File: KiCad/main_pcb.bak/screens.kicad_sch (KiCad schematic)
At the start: 15 parts, among them J7 1X7 Header, J8 1X7 Header, J9 1x13 Header, U4 TI TXB0104DR, U6 TI TXB0104DR, U9 TI TXB0104DR

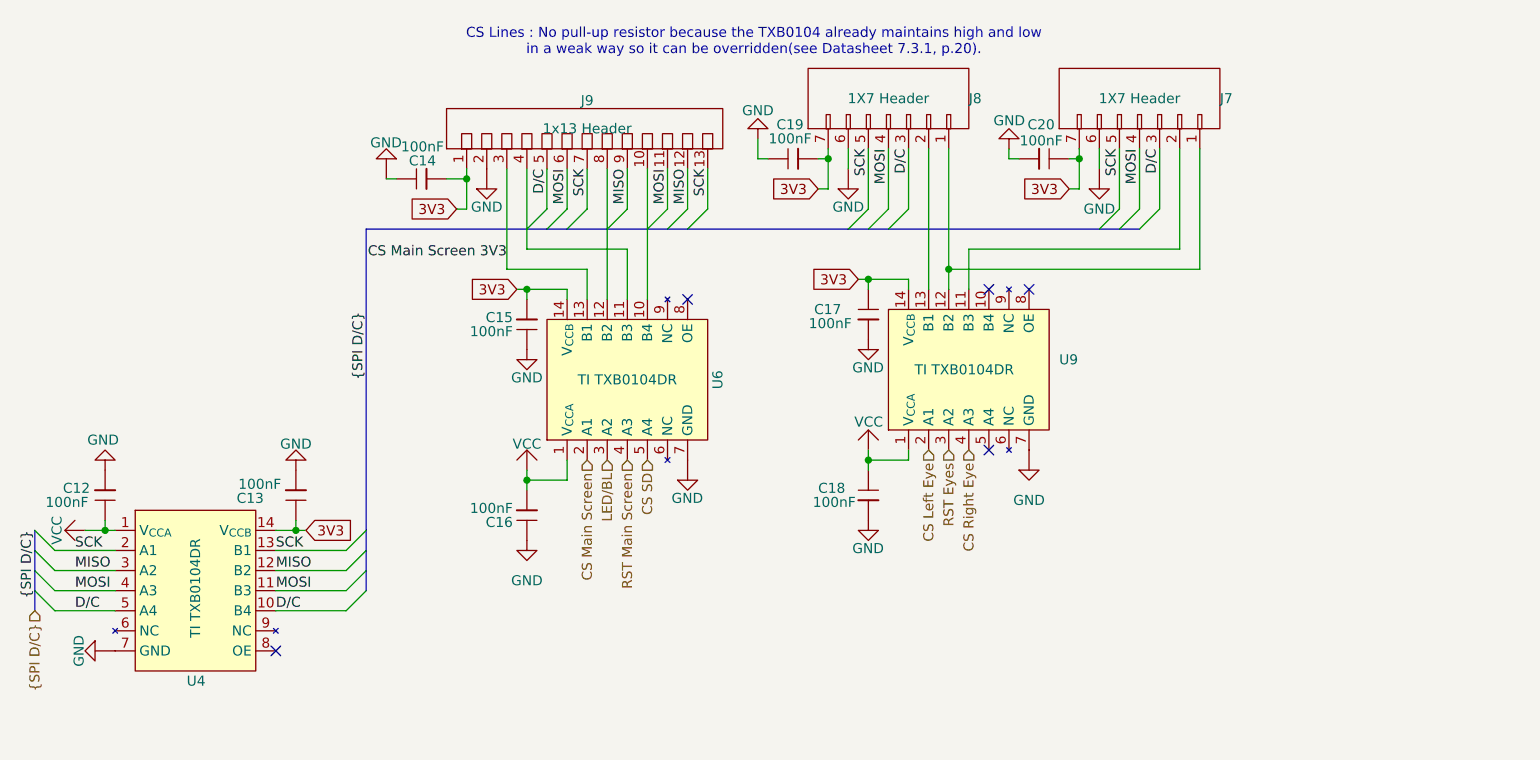
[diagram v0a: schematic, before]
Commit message: Maddie/main pcb refactor (#39)
* feat(PCB Layout): Refactors Main PCB layout to achieve smaller form factor and adds JLCPCB constraints.

* feat(symbols): Adds 4pin crystal symbols and adds it to schematic

* feat(schematic): Connects C2 and C3 to the crystal

* feat(schematic): Revamps fully the circuit schematic

* feat(schematic): Assigns footprints to symbols

* feat(pcb): Alternative first draft

* feat(pcb): Second draft

* feat(pdf): Updates schematic PDF

* feat(pdf): Updates schematic PDF

* chore(migration): Puts old layout in main_pcb.bak/ and new layout to main_pcb/

* feat(PCB): Updates PCB layout after Christian's review, thansk a lot Christian :) !
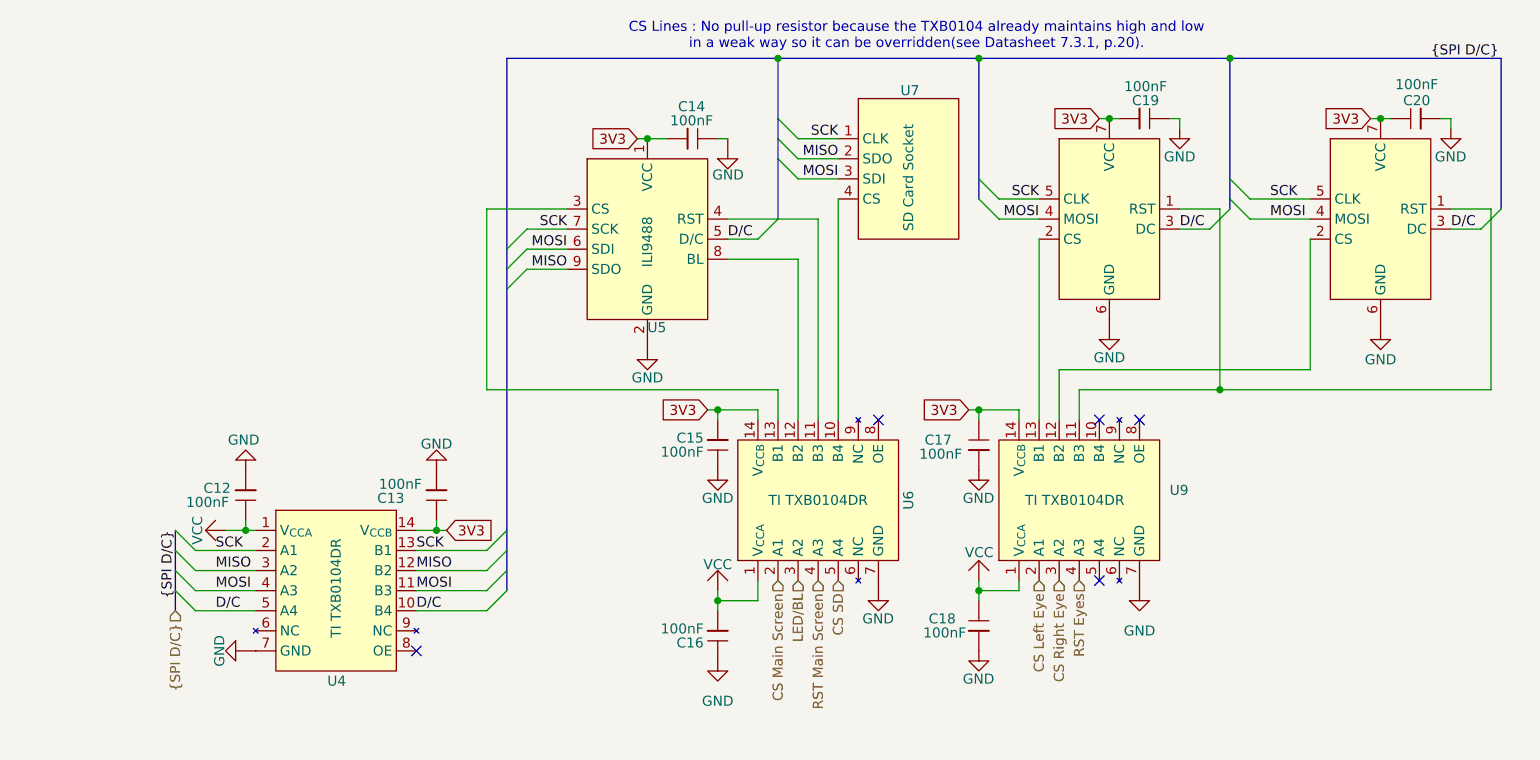
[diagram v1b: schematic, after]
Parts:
- removed J7, J8: 1X7 Header, Lilibrary:1x7 Header, symbol Lily's Pad:1x7_Header
- removed J9: 1x13 Header, Lilibrary:1x13 Header, symbol Lily's Pad:1x13_Header
- added U10, U8: ~, symbol Lily's Pad:GC9A01
- added U5: ILI9488, symbol Lily's Pad:ILI9488
- added U7: SD Card Socket, symbol Lily's Pad:SD_Card_Socket
- C12, C13, C14, C15, C16, C17, C18, C19, C20: footprint Capacitor_SMD:C_0603_1608Metric_Pad1.08x0.95mm_HandSolder -> Capacitor_SMD:C_0201_0603Metric_Pad0.64x0.40mm_HandSolder
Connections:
- net 3V3: now also U10.7 (VCC), U5.1 (VCC), U8.7 (VCC)
- net CS Right Eye: now also U9.3 (A2); no longer U9.4 (A3)
- net D/C: now also U10.3 (DC), U5.5 (D/C), U8.3 (DC)
- net GND: now also U10.6 (GND), U5.2 (GND), U8.6 (GND)
- net MISO: now also U5.9 (SDO), U7.2 (SDO)
- net MOSI: now also U10.4 (MOSI), U5.6 (SDI), U7.3 (SDI), U8.4 (MOSI)
- net RST Eyes: now also U9.4 (A3); no longer U9.3 (A2)
- net SCK: now also U10.5 (CLK), U5.7 (SCK), U7.1 (CLK), U8.5 (CLK)
- net at U9.11 (B3): now also U10.1 (RST), U8.1 (RST)
- net at U9.12 (B2): now also U10.2 (CS)
- net at U9.13 (B1): now also U8.2 (CS)
- net at U6.10 (B4): now also U7.4 (CS)
- net at U6.11 (B3): now also U5.4 (RST)
- net at U6.12 (B2): now also U5.8 (BL)
- net CS Main Screen 3V3: no longer names the net of U6.13 (B1)
- net CS Main Screen 3V3: now also U5.3 (CS)
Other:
- moved on the sheet: C12, C13, C14, C15, C16, C17, C18, C19, C20, U4, U6, U9
